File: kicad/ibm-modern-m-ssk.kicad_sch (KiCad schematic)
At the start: 20 parts, among them J1 USB_C_Receptacle_USB2.0_14P, J2 Conn_01x02_Socket, J3 Conn_02x06_Odd_Even, U1 MDBT50Q-1MV2, U2 MCP73831T-2ACI/OT, U3 XC6206P332MR, U4 USBLC6-2P6, Y1 32MHz

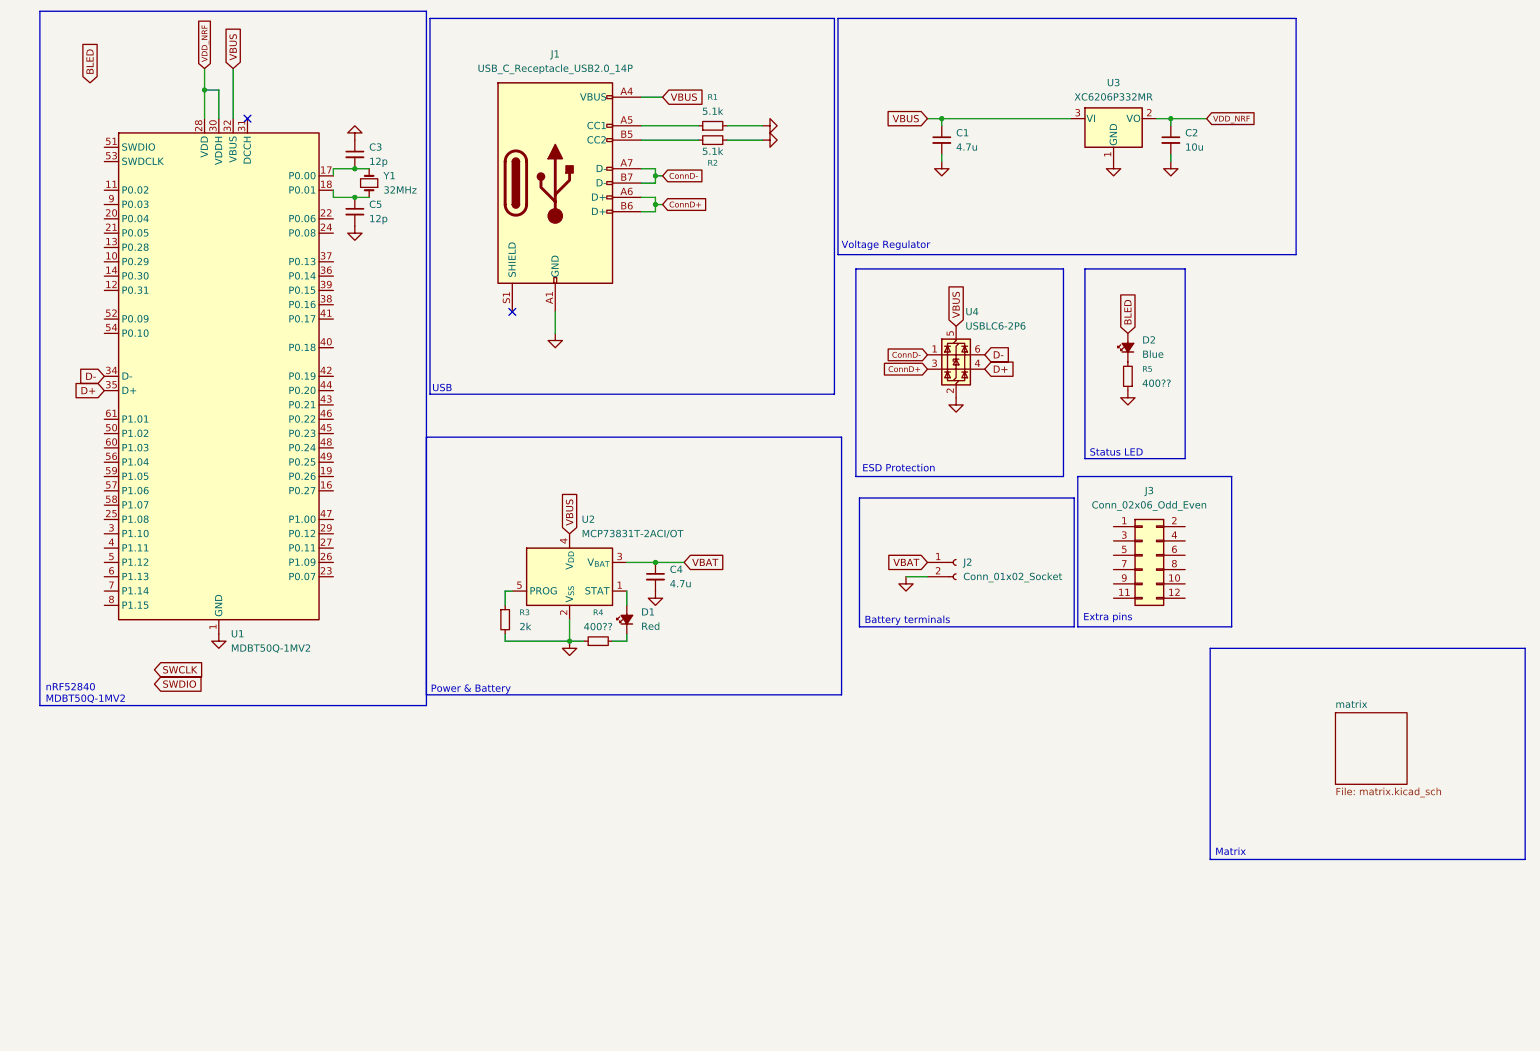
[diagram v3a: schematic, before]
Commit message: Schematic done
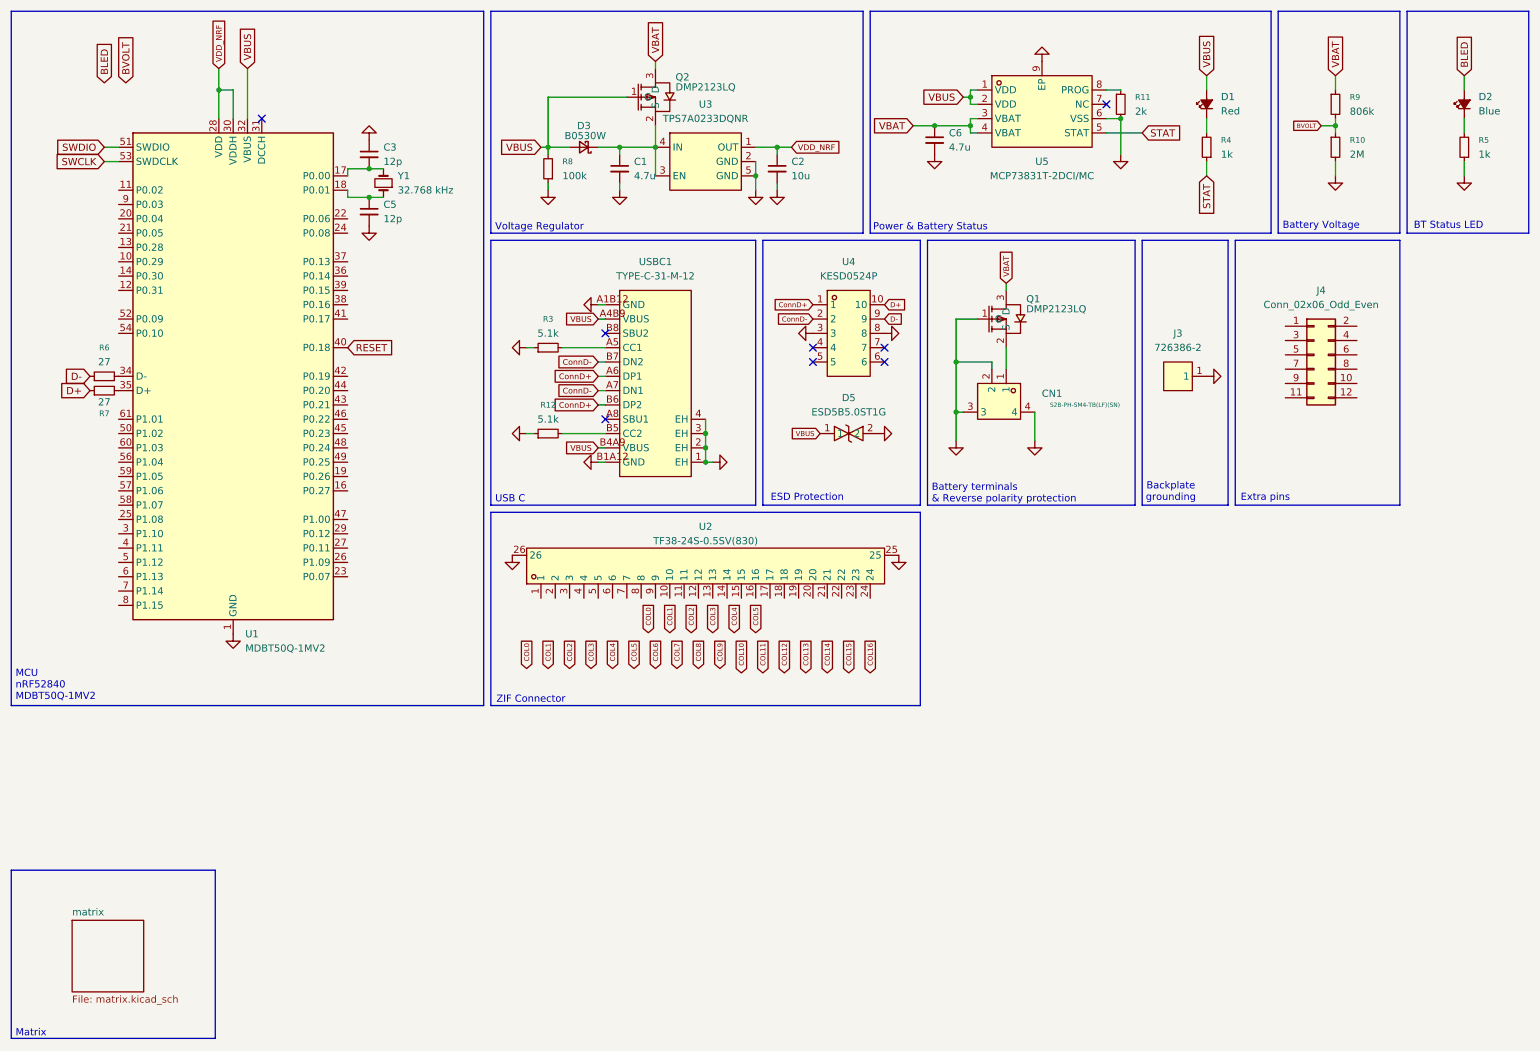
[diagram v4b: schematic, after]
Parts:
- removed C4: 4.7u, symbol Device:C_Small
- removed J1: USB_C_Receptacle_USB2.0_14P, PCM_marbastlib-various:USB_C_Receptacle_HRO_TYPE-C-31-M-12, symbol Connector:USB_C_Receptacle_USB2.0_14P
- removed J2: Conn_01x02_Socket, symbol Connector:Conn_01x02_Socket
- removed R1, R2: 5.1k, symbol Device:R_Small
- removed U2: MCP73831T-2ACI/OT, Package_TO_SOT_SMD:SOT-23-5, symbol Battery_Management:MCP73831-2-OT
- removed U3: XC6206P332MR, Package_TO_SOT_SMD:SOT-23-3, symbol Regulator_Linear:XC6206PxxxMR
- removed U4: USBLC6-2P6, Package_TO_SOT_SMD:SOT-666, symbol Power_Protection:USBLC6-2P6
- added C6: 4.7u, symbol Device:C_Small
- added CN1: S2B-PH-SM4-TB(LF)(SN), easyeda2kicad:CONN-SMD_P2.00_S2B-PH-SM4-TB-LF-SN, symbol easyeda2kicad:S2B-PH-SM4-TB(LF)(SN)
- added D3: B0530W, easyeda2kicad:SOD-123_L2.8-W1.8-LS3.7-RD, symbol Device:D_Schottky_Small
- added D5: ESD5B5.0ST1G, easyeda2kicad:SOD-523_L1.2-W0.8-LS1.6-BI, symbol easyeda2kicad:ESD5B5.0ST1G
- added J3: 726386-2, easyeda2kicad:CONN-TH_726386-2, symbol easyeda2kicad:726386-2
- added Q1, Q2: DMP2123LQ, easyeda2kicad:SOT-23-3_L2.9-W1.3-P1.90-LS2.4-BR, symbol easyeda2kicad:DMP2123LQ
- added R10: 2M, symbol Device:R_Small
- added R11: 2k, symbol Device:R_Small
- added R12: 5.1k, symbol Device:R_Small
- added R6, R7: 27, symbol Device:R_Small
- added R8: 100k, symbol Device:R_Small
- added R9: 806k, symbol Device:R_Small
- added U2: TF38-24S-0.5SV(830), easyeda2kicad:FPC-SMD_24P-P0.50_TF38-24S-0.5SV-830, symbol easyeda2kicad:TF38-24S-0.5SV(830)
- added U3: TPS7A0233DQNR, easyeda2kicad:X2SON-4_L1.0-W1.0-P0.65-TL-EP, symbol easyeda2kicad:TPS7A0233DQNR
- added U4: KESD0524P, easyeda2kicad:DFN2510-10_L2.5-W1.0-P0.50-BL, symbol easyeda2kicad:KESD0524P
- added U5: MCP73831T-2DCI/MC, easyeda2kicad:DFN-8_L3.0-W2.0-P0.50-BL-EP1.6, symbol easyeda2kicad:MCP73831T-2DCI_MC
- added USBC1: TYPE-C-31-M-12, easyeda2kicad:USB-C_SMD-TYPE-C-31-M-12_1, symbol easyeda2kicad:TYPE-C-31-M-12
- R3: value 2k -> 5.1k
- R4, R5: value 400?? -> 1k
- Y1: value 32MHz -> 32.768 kHz
- renumbered J3 to J4
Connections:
- net ConnD+: now also U4.1, USBC1.A6 (DP1), USBC1.B6 (DP2)
- net ConnD-: now also U4.2, USBC1.A7 (DN1), USBC1.B7 (DN2)
- net D+: now also R7.1, U4.10; no longer U1.35 (D+)
- net D-: now also R6.1, U4.9; no longer U1.34 (D-)
- net GND: now also R3.1, C6.2, CN1.2, CN1.3, CN1.4, D5.2, J3.1, Q1.1 (G), R10.2, R11.2, R12.1, R8.1, U2.25, U2.26, U3.2 (GND), U3.5 (GND), U4.3, U4.8, U5.6 (VSS), U5.9 (EP), USBC1.1 (EH), USBC1.2 (EH), USBC1.3 (EH), USBC1.4 (EH), USBC1.A1B12 (GND), USBC1.B1A12 (GND); no longer R3.2, R4.1
- net SWCLK: now also U1.53 (SWDCLK)
- net SWDIO: now also U1.51 (SWDIO)
- net VBAT: now also C6.1, Q1.3 (D), Q2.3 (D), R9.1, U5.3 (VBAT), U5.4 (VBAT)
- net VBUS: now also D1.2 (A), D3.2 (A), D5.1, Q2.1 (G), R8.2, U5.1 (VDD), U5.2 (VDD), USBC1.A4B9 (VBUS), USBC1.B4A9 (VBUS); no longer C1.1
- net VDD_NRF: now also U3.1 (OUT)
- net RESET: now reaches U1.40 (P0.18)
- new net: C1.1, D3.1 (K), Q2.2 (S), U3.3 (EN), U3.4 (IN)
- new net: R11.1, U5.8 (PROG)
- new net: R3.2, USBC1.A5 (CC1)
- new net: R12.2, USBC1.B5 (CC2)
- new net: CN1.1, Q1.2 (S)
- new net: R6.2, U1.34 (D-)
- new net: R7.2, U1.35 (D+)
- new net BVOLT: R10.1, R9.2
- new net STAT: R4.1, U5.5 (STAT)
- no-connect marks 2 -> 8
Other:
- note added: "BT Status LED"
- note added: "Backplate grounding"
- note added: "Battery Voltage"
- note added: "Battery terminals & Reverse polarity protection"
- note added: "MCU nRF52840 MDBT50Q-1MV2"
- note added: "Power & Battery Status"
- note added: "USB C"
- note added: "ZIF Connector"
- note removed: "Battery terminals"
- note removed: "Power & Battery"
- note removed: "Status LED"
- note removed: "USB"
- note removed: "nRF52840 MDBT50Q-1MV2"
- moved on the sheet: C1, C2, C3, C5, D1, D2, J4, R4, R5, U1, Y1

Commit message: Schematic Done v2
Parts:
- added J5: Conn_01x04_Pin, Connector_PinHeader_2.54mm:PinHeader_1x04_P2.54mm_Vertical, symbol Connector:Conn_01x04_Pin
- added SW89: SW_Push, easyeda2kicad:SW-SMD_L3.9-W3.0-P4.45, symbol Switch:SW_Push
- D1, D2: symbol Device:LED_Small_Filled -> Device:LED_Small
- renumbered C6 to C1, C3 to C2, C1 to C3, C2 to C4, D5 to D4, CN1 to J1, J3 to J2, U2 to J3, Q2 to Q1, Q1 to Q2, R11 to R1, R12 to R10, R9 to R2, R4 to R3, R10 to R4, R8 to R6, R3 to R7, R6 to R8, R7 to R9, U5 to U1, U3 to U2, U4 to U3, U1 to U4
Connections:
- net GND: now also J5.4 (Pin_4), SW89.2
- net RESET: now also SW89.1
- net SWCLK: now also J5.2 (Pin_2)
- net SWDIO: now also J5.3 (Pin_3)
- net VDD_NRF: now also J5.1 (Pin_1)
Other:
- note added: "SWD Programming & Reset"
- moved on the sheet: J4

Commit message: Footprints & BOM done
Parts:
- C1, C3: footprint (none) -> Capacitor_SMD:C_0201_0603Metric; LCSC Part (none) -> C19666
- C2, C5: footprint (none) -> Capacitor_SMD:C_0201_0603Metric; LCSC Part (none) -> C38523
- C4: footprint (none) -> Capacitor_SMD:C_0201_0603Metric; LCSC Part (none) -> C1634
- D1: footprint (none) -> LED_SMD:LED_0201_0603Metric; LCSC Part (none) -> C2286
- D2: footprint (none) -> LED_SMD:LED_0201_0603Metric; LCSC Part (none) -> C2288
- J4, J5: now left out of the parts list
- R1: footprint (none) -> Resistor_SMD:R_0402_1005Metric; LCSC Part (none) -> C60488
- R10, R7: footprint (none) -> Resistor_SMD:R_0402_1005Metric; LCSC Part (none) -> C105872
- R2: footprint (none) -> Resistor_SMD:R_0402_1005Metric; LCSC Part (none) -> C375495
- R3: footprint (none) -> Resistor_SMD:R_0402_1005Metric; LCSC Part (none) -> C105637
- R4: footprint (none) -> Resistor_SMD:R_0402_1005Metric; LCSC Part (none) -> C138014
- R5: value 1k -> 470; footprint (none) -> Resistor_SMD:R_0402_1005Metric; LCSC Part (none) -> C114877
- R6: footprint (none) -> Resistor_SMD:R_0402_1005Metric; LCSC Part (none) -> C60491
- R8, R9: footprint (none) -> Resistor_SMD:R_0402_1005Metric; LCSC Part (none) -> C137890
- U4: LCSC Part (none) -> C5118826
- Y1: footprint (none) -> easyeda2kicad:FC-135R_L3.2-W1.5; LCSC Part (none) -> C32346

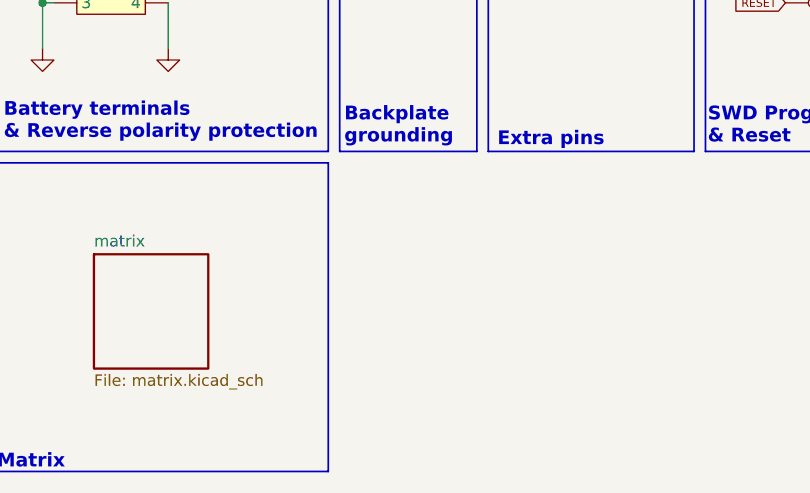
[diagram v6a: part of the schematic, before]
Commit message: Import complete KiCad PCB, schematic & footprint
Add full KiCad PCB file (ibm-modern-m-ssk.kicad_pcb) including board setup, layers, nets and populated footprints (generated by pcbnew 9.0). Update project files (.kicad_prl, .kicad_pro, .kicad_sch) to match the imported board. Add new pretty library footprint easyeda2kicad.pretty/CONN-SMD_2P-P1.00_SM02B-SRSS-TB-LF-SN.kicad_mod referenced by the board.
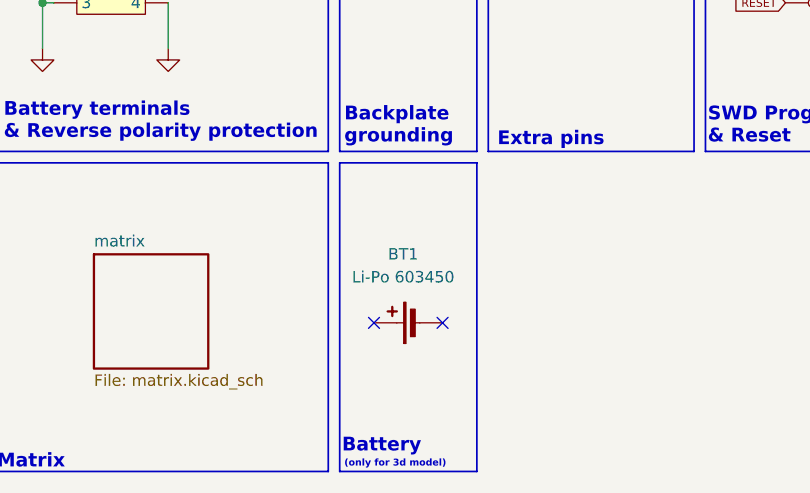
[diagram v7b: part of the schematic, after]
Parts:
- added BT1: Li-Po 603450, easyeda2kicad:LiPo_603450, symbol Device:Battery_Cell
- J1: footprint easyeda2kicad:CONN-SMD_P2.00_S2B-PH-SM4-TB-LF-SN -> easyeda2kicad:CONN-SMD_2P-P1.00_SM02B-SRSS-TB-LF-SN; LCSC Part C295747 -> C160402
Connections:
- no-connect marks 8 -> 10
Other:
- note added: "(only for 3d model)"
- note added: "Battery"
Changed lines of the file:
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@@
 	)
 	(rectangle
+		(start 214.63 102.87)
+		(end 229.87 137.16)
+		(stroke
+			(width 0.1905)
+			(type default)
+		)
+		(fill
+			(type none)
+		)
+	)
+	(rectangle
 		(start 231.14 54.61)
 		(end 254 101.6)
@@
 		)
 	)
+	(text "(only for 3d model)"
+		(exclude_from_sim no)
+		(at 215.138 136.398 0)
+		(effects
+			(font
+				(size 0.762 0.762)
+				(thickness 0.3048)
+				(bold yes)
+			)
+			(justify left)
+		)
+	)
+	(text "Battery"
+		(exclude_from_sim no)
+		(at 214.884 134.366 0)
+		(effects
+			(font
+				(size 1.524 1.524)
+				(thickness 0.3048)
+				(bold yes)
+			)
+			(justify left)
+		)
+	)
 	(text "ZIF Connector"
 		(exclude_from_sim no)
@@
 	)
 	(no_connect
+		(at 226.06 120.65)
+	)
+	(no_connect
 		(at 119.38 86.36)
 	)
@@
 		(at 208.28 30.48)
 	)
+	(no_connect
+		(at 218.44 120.65)
+	)
 	(wire
 		(pts
@@
 			)
 		)
-		(property "Footprint" "easyeda2kicad:CONN-SMD_P2.00_S2B-PH-SM4-TB-LF-SN"
+		(property "Footprint" "easyeda2kicad:CONN-SMD_2P-P1.00_SM02B-SRSS-TB-LF-SN"
 			(at 175.26 81.28 0)
 			(effects
@@
 			)
 		)
-		(property "Datasheet" "https://www.lcsc.com/product-detail/_JST-Sales-America_S2B-PH-SM4-TB-LF-SN_JST-Sales-America-S2B-PH-SM4-TB-LF-SN_C295747.html"
+		(property "Datasheet" "https://www.lcsc.com/product-detail/C160402.html"
 			(at 172.72 81.28 0)
 			(effects
@@
 			)
 		)
-		(property "LCSC Part" "C295747"
+		(property "LCSC Part" "C160402"
 			(at 170.18 81.28 0)
 			(effects
@@
 					(unit 1)
 				)
+			)
+		)
+	)
+	(symbol
+		(lib_id "Device:Battery_Cell")
+		(at 223.52 120.65 90)
+		(unit 1)
+		(exclude_from_sim no)
+		(in_bom yes)
+		(on_board yes)
+		(dnp no)
+		(fields_autoplaced yes)
+		(property "Reference" "BT1"
+			(at 221.6785 113.03 90)
+			(effects
+				(font
+					(size 1.27 1.27)
+				)
+			)
+		)
+		(property "Value" "Li-Po 603450"
+			(at 221.6785 115.57 90)
+			(effects
+				(font
+					(size 1.27 1.27)
+				)
+			)
+		)
+		(property "Footprint" "easyeda2kicad:LiPo_603450"
+			(at 221.996 120.65 90)
+			(effects
+				(font
+					(size 1.27 1.27)
+				)
+				(hide yes)
+			)
+		)
+		(property "Datasheet" "~"
+			(at 221.996 120.65 90)
+			(effects
+				(font
+					(size 1.27 1.27)
+				)
+				(hide yes)
+			)
+		)
+		(property "Description" "Single-cell battery"
+			(at 223.52 120.65 0)
+			(effects
+				(font
+					(size 1.27 1.27)
+				)
+				(hide yes)
+			)
+		)
+		(pin "1"
+		)
+		(pin "2"
+		)
+		(instances
+			(project ""
+				(path "/17f6a4a5-fbff-4e30-a1cc-9481373e4968"
+					(reference "BT1")
+					(unit 1)
+				)

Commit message: update
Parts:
- removed D2: Blue, LED_SMD:LED_0201_0603Metric, symbol Device:LED_Small
- removed R4: 2M, Resistor_SMD:R_0402_1005Metric, symbol Device:R_Small
- removed R5: 470, Resistor_SMD:R_0402_1005Metric, symbol Device:R_Small
- added C10, C9: 10u, Capacitor_SMD:C_0201_0603Metric, symbol Device:C_Small
- added C6, C8: 1u, Capacitor_SMD:C_0201_0603Metric, symbol Device:C_Small
- added C7: 4.7u, Capacitor_SMD:C_0201_0603Metric, symbol Device:C_Small
- added E1: PESD5V0S1BL,315, easyeda2kicad:SOD-882_L1.0-W0.6-BI, symbol Device:D_TVS_Small
- added E2: TPD2E001DRYR-TP, easyeda2kicad:SON-6_L1.4-W1.0-P0.50-TL_USBULC6-2M6, symbol easyeda2kicad:TPD2E001DRYR-TP
- added R11, R15: 4.7k, Resistor_SMD:R_0402_1005Metric, symbol Device:R_Small
- added R12: 47k, Resistor_SMD:R_0402_1005Metric, symbol Device:R_Small
- added R13: 1.8k, Resistor_SMD:R_0402_1005Metric, symbol Device:R_Small
- added R14: 10k, Resistor_SMD:R_0402_1005Metric, symbol Device:R_Small
- added SW90: SW_SPDT, symbol Switch:SW_SPDT
- added U5: XC6220B331ER-G, easyeda2kicad:USP-6C_L2.0-W1.8-P0.50-BL-EP, symbol easyeda2kicad:XC6220B331ER-G
- added U6: BQ24075RGTR, easyeda2kicad:QFN-16_L3.0-W3.0-P0.50-TL-EP1.7, symbol easyeda2kicad:BQ24075RGTR
- added U7: LC709203FXE-03MH, easyeda2kicad:WLCSP-9_L1.6-W1.8-R3-C3-P0.50-BL, symbol easyeda2kicad:LC709203FXE-03MH
- R2: value 806k -> 10k; LCSC Part C375495 -> C105637
- R3: value 1k -> 1.5k
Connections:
- net BVOLT is gone; now on net GND: R2.2
- net D+ is gone; now on net ConnD+: R9.1, U3.10
- net D- is gone; now on net ConnD-: R8.1, U3.9
- net ConnD+: now also E2.3 (IO1)
- net ConnD-: now also E2.6 (IO2)
- net GND: now also C10.2, C6.2, C7.2, C8.2, C9.2, E1.1 (A1), E2.4 (GND), R12.1, R13.1, R14.1, U5.4 (VSS), U5.7 (EP), U6.17 (EP), U6.4 (#CE), U6.5 (EN2), U6.8 (VSS), U7.A1 (VSS), U7.B1 (TEST)
- net STAT: no longer R3.1
- net VBAT: now also C8.1, U6.2 (BAT), U6.3 (BAT), U7.A3 (VDD); no longer R2.1
- net VDD_NRF: now also C10.1, R11.2, R15.2, U5.1 (VOUT), U5.2 (VOUT)
- net at D1.1 (K): now also R3.1; no longer R3.2
- net VBUS renamed ConnVBUS
- net ConnVBUS: now also C6.1, E1.2 (A2), E2.1 (VCC), U6.13 (IN), U6.6 (EN1); no longer D1.2 (A)
- new net: R14.2, SW90.1 (A)
- new net: R3.2, U6.9 (#CHG)
- new net: R2.1, U7.C3 (TSENSE)
- new net: R13.2, U6.16 (ISET)
- new net: R12.2, U6.14 (TMR)
- new net BAT_NTC: SW90.3 (C)
- new net SCL: R11.1, U7.C2 (SCL)
- new net SDA: R15.1, U7.C1 (SDA)
- new net SYS_POWER: C7.1, D1.2 (A), U6.10 (OUT), U6.11 (OUT)
- new net SYS_PWR: C9.1, U5.3 (CE), U5.5 (VIN), U5.6 (VIN)
- new net TSENS: SW90.2 (B), U6.1 (TS)
- no-connect marks 10 -> 18
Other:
- note added: "3V3 LDO Regulator"
- note added: "Battery Fuel Gauge"
- note added: "MCU nRF52840 MDBT50Q-U1MV2"
- note added: "NTC Selector"
- note added: "Power Path & Charger"
- note added: "check if footprint pins are correct!!!!"
- note removed: "BT Status LED"
- note removed: "Battery Voltage"
- note removed: "MCU nRF52840 MDBT50Q-1MV2"
- moved on the sheet: BT1, C1, C2, C3, C4, C5, D1, D3, D4, J1, J2, J3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
